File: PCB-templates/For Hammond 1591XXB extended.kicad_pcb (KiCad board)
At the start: 2 copper layers, 90.5 x 56 mm, 0 parts

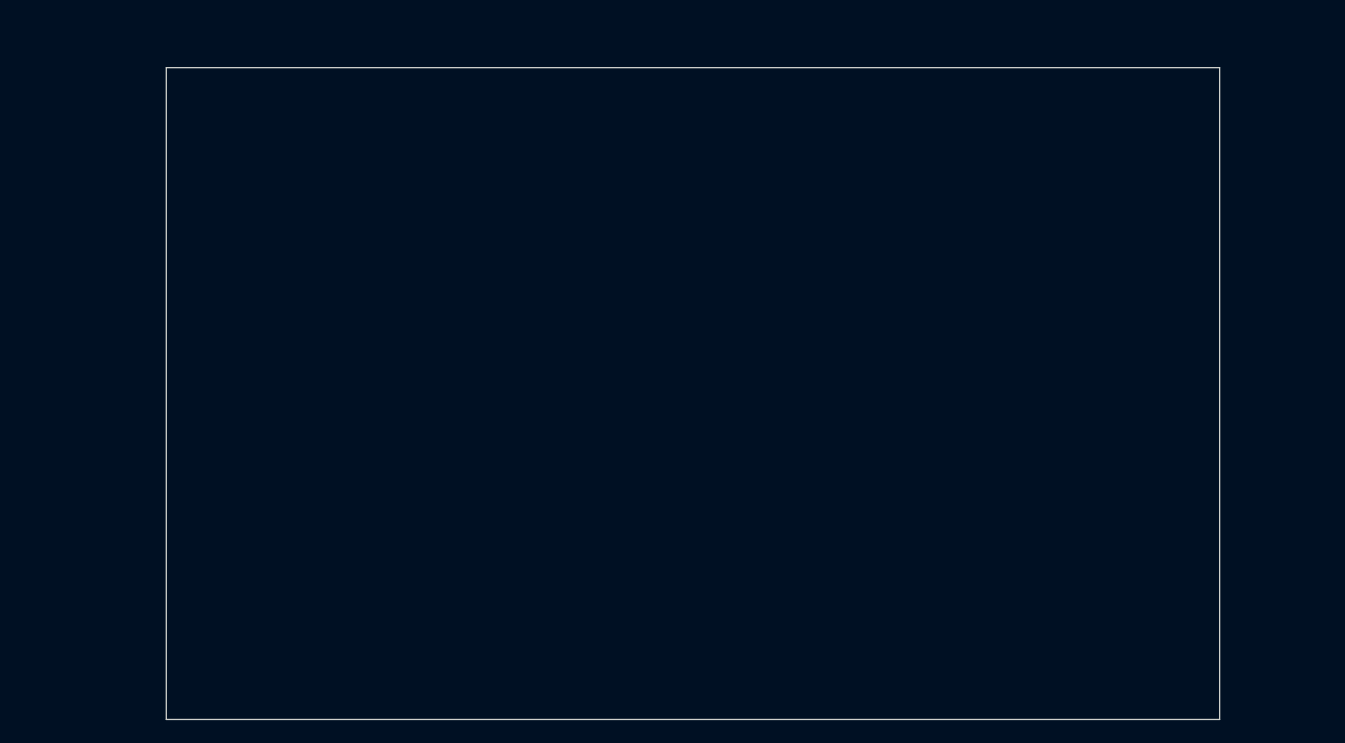
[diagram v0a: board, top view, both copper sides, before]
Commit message: More PCB templates for Hammond 1591XX case, extended with more room + p44 shield
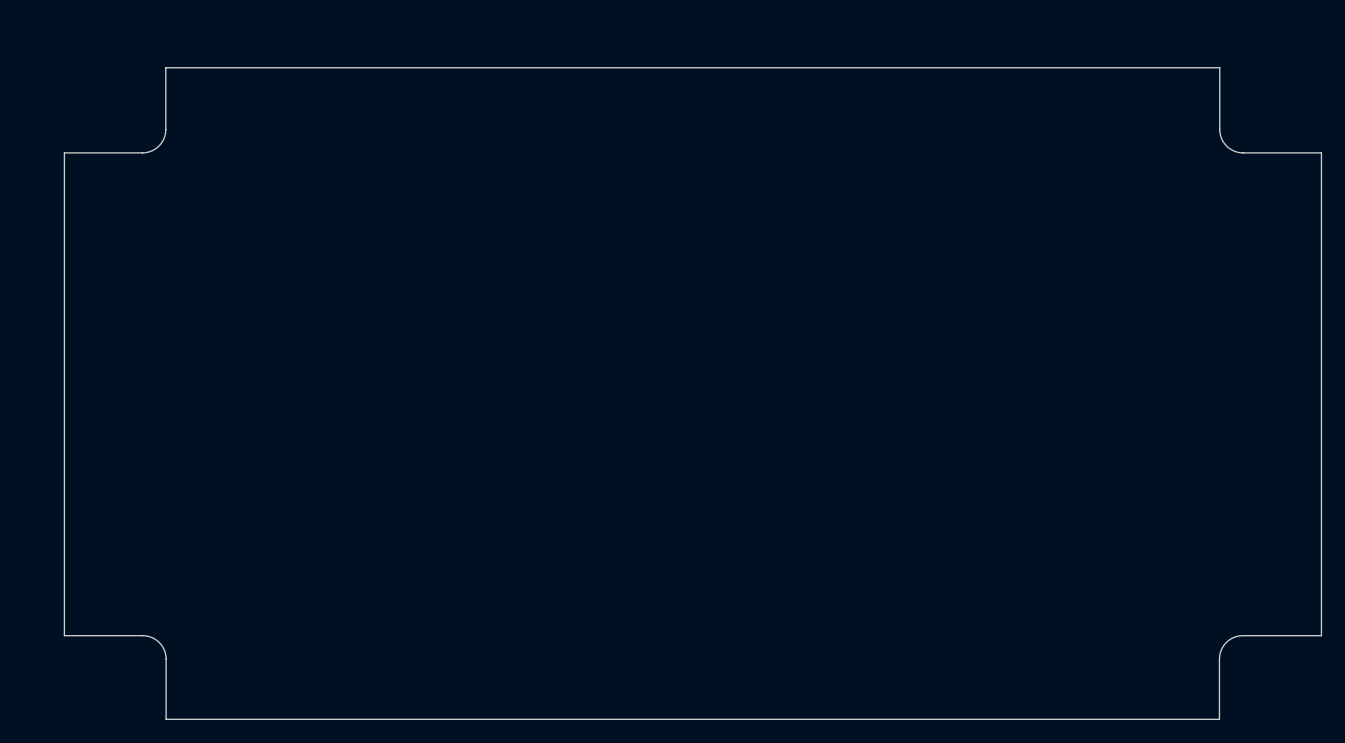
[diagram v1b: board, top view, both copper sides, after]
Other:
- board size 90.5 x 56 mm -> 108 x 56 mm
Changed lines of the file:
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@@
   (general
     (thickness 1.6)
-    (drawings 22)
+    (drawings 34)
     (tracks 0)
     (zones 0)
@@
     (uvia_drill 0.1)
   )
+  (gr_line (start 162.5092 69.3166) (end 162.5092 64.008) (layer Edge.Cuts) (width 0.1))
+  (gr_line (start 164.5158 71.3232) (end 171.2468 71.3232) (layer Edge.Cuts) (width 0.1))
+  (gr_line (start 164.4904 112.8014) (end 171.2468 112.8014) (layer Edge.Cuts) (width 0.1))
+  (gr_line (start 162.4838 119.9896) (end 162.4838 114.808) (layer Edge.Cuts) (width 0.1))
+  (gr_line (start 69.977 112.8014) (end 63.246 112.8014) (layer Edge.Cuts) (width 0.1))
+  (gr_line (start 71.9836 114.808) (end 71.9836 119.9896) (layer Edge.Cuts) (width 0.1))
+  (gr_arc (start 164.5158 69.3166) (end 162.5092 69.3166) (angle -90) (layer Edge.Cuts) (width 0.1))
+  (gr_arc (start 164.4904 114.808) (end 164.4904 112.8014) (angle -90) (layer Edge.Cuts) (width 0.1))
+  (gr_arc (start 69.977 114.808) (end 71.9836 114.808) (angle -90) (layer Edge.Cuts) (width 0.1))
+  (gr_line (start 69.9516 71.3232) (end 63.246 71.3232) (layer Edge.Cuts) (width 0.1))
+  (gr_line (start 71.9582 64.008) (end 71.9582 69.3166) (layer Edge.Cuts) (width 0.1))
+  (gr_arc (start 69.9516 69.3166) (end 69.9516 71.3232) (angle -90) (layer Edge.Cuts) (width 0.1))
+  (gr_line (start 71.9582 64.008) (end 162.5092 64.008) (layer Edge.Cuts) (width 0.1))
+  (gr_line (start 171.2468 112.8014) (end 171.2468 71.3232) (layer Edge.Cuts) (width 0.1))
+  (gr_line (start 71.9836 119.9896) (end 162.4838 119.9896) (layer Edge.Cuts) (width 0.1))
+  (gr_line (start 63.246 71.3232) (end 63.246 112.8014) (layer Edge.Cuts) (width 0.1))
   (gr_circle (center 156.0322 110.2868) (end 160.02 110.3122) (layer Dwgs.User) (width 0.15))
   (gr_circle (center 156.0322 110.2868) (end 157.8102 110.2614) (layer Dwgs.User) (width 0.15))
@@
   (gr_circle (center 78.5 73.8) (end 82.423 73.787) (layer Dwgs.User) (width 0.15))
   (gr_circle (center 78.5 73.8) (end 80.264 73.787) (layer Dwgs.User) (width 0.15))
-  (gr_line (start 72 120) (end 72 64) (angle 90) (layer Edge.Cuts) (width 0.1))
-  (gr_line (start 162.5 120) (end 72 120) (angle 90) (layer Edge.Cuts) (width 0.1))
-  (gr_line (start 162.5 64) (end 162.5 120) (angle 90) (layer Edge.Cuts) (width 0.1))
-  (gr_line (start 72 64) (end 162.5 64) (angle 90) (layer Edge.Cuts) (width 0.1))
   (dimension 108 (width 0.3) (layer Dwgs.User)
     (gr_text "108.000 mm" (at 117.25 36.75) (layer Dwgs.User)

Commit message: Templates for Hammond 1591XXB redrawn, higher precision
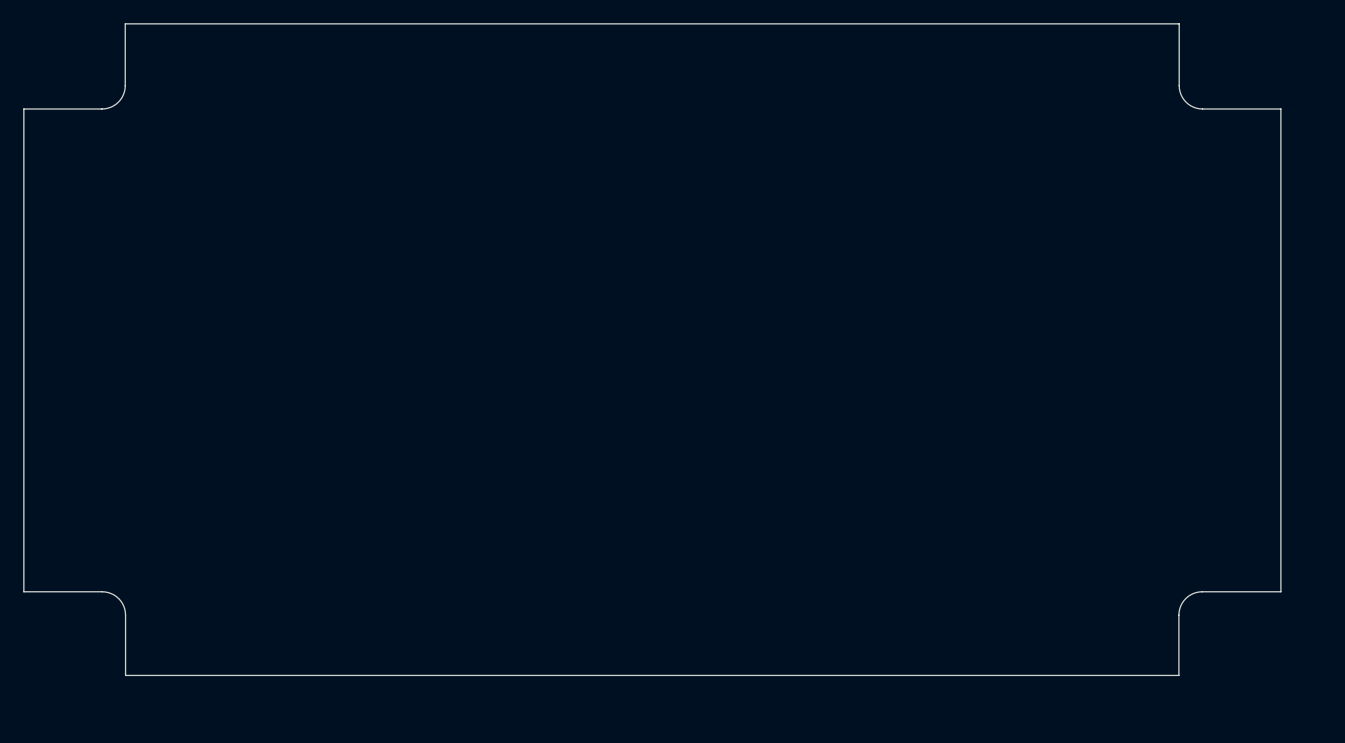
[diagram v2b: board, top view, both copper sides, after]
